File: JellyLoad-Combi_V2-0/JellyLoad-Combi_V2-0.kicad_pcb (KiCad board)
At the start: 2 copper layers, 26 x 35 mm, 26 parts, among them J1 Conn_02x07_Odd_Even, Q1 SFH3710, Q2 SFH3710, Q3 SFH3710, Q4 SFH3710, Q5 SFH3710, Q6 SFH3710, Q7 SFH3710, Q8 SFH3710, Q9 SFH3710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

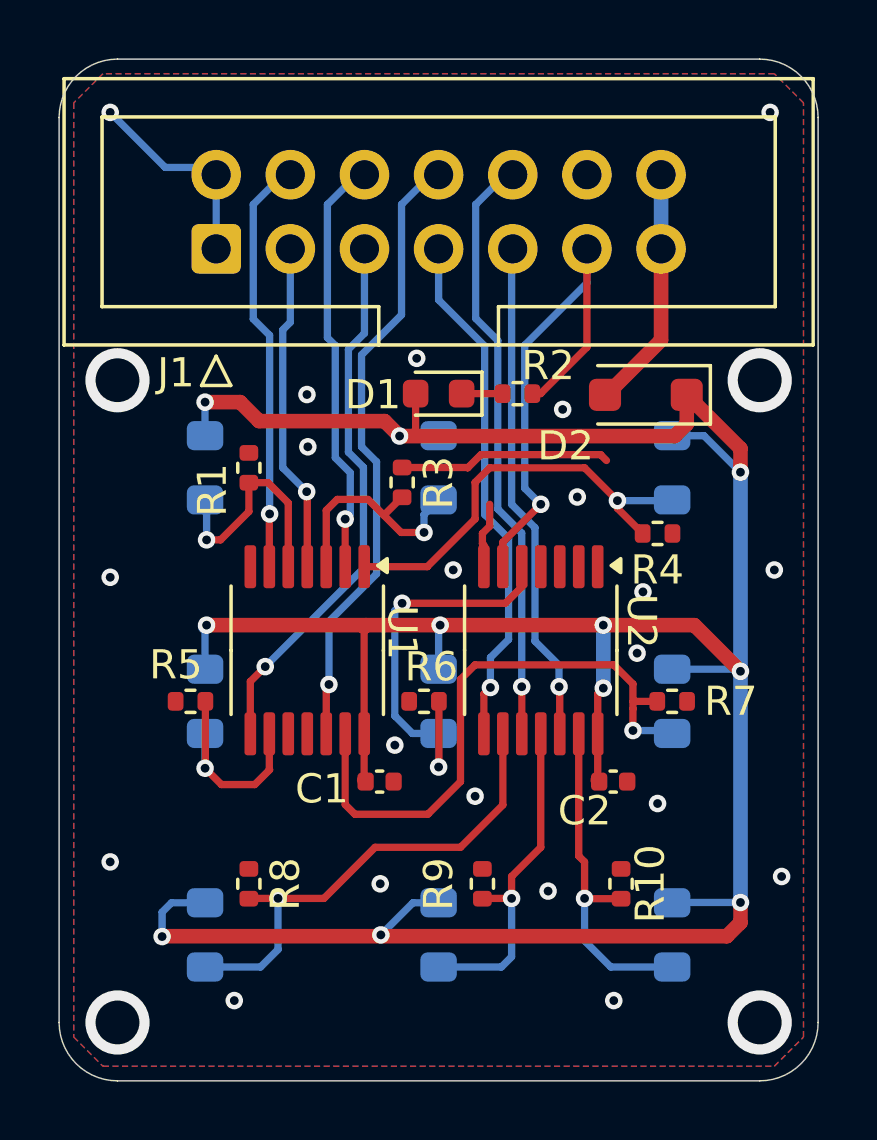
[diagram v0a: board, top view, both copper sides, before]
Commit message: Layout updates for manufacture process
Corner mounting holes widened to 2.0mm for more robust mechanics. Added 2x tooling holes (1.152mm) for assembly process.
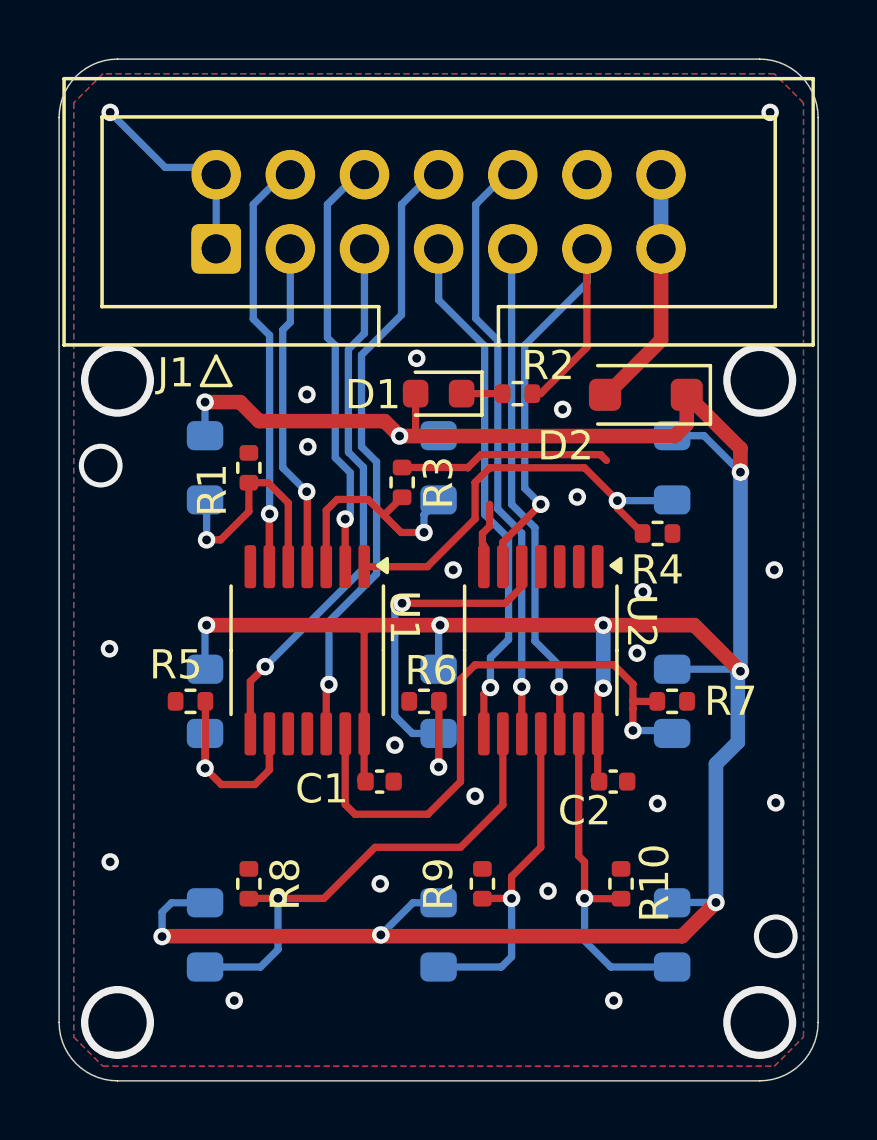
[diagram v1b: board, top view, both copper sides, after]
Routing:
- net VCC: track 106.7 -> 105.0 mm
- net GND: vias 25 -> 27
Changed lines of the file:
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@@
 		(grid_origin 170 107)
 		(pcbplotparams
-			(layerselection 0x00014dc_ffffffff)
-			(plot_on_all_layers_selection 0x0000000_00000000)
+			(layerselection 0x00010dc_ffffffff)
+			(plot_on_all_layers_selection 0x0001000_00000000)
 			(disableapertmacros no)
 			(usegerberextensions no)
@@
 		(tags "resistor")
 		(property "Reference" "R10"
-			(at 0 1 90)
+			(at 0.025 1.15 90)
 			(layer "F.SilkS")
 			(effects
@@
 		(tags "TSSOP SO")
 		(property "Reference" "U1"
-			(at -0.606 -3.25 -90)
+			(at -1.125 -3.325 -90)
 			(unlocked yes)
 			(layer "F.SilkS")
@@
 		(tags "resistor")
 		(property "Reference" "R6"
-			(at -0.25 1.182 0)
+			(at -0.25 1.05 0)
 			(layer "F.SilkS")
 			(effects
@@
 	)
 	(via
-		(at 158.75 102.75)
+		(at 181.55 110.475)
 		(size 0.6)
 		(drill 0.3)
@@
 	)
 	(via
+		(at 158.425 98.925)
+		(size 1.5)
+		(drill 1.152)
+		(layers "F.Cu" "B.Cu")
+		(net 1)
+	)
+	(via
 		(at 181.356 86.8255)
 		(size 0.6)
@@
 	(via
 		(at 159 96)
-		(size 2.2)
-		(drill 1.5)
+		(size 2.5)
+		(drill 2)
 		(layers "F.Cu" "B.Cu")
 		(net 1)
@@
 	(via
 		(at 181 96)
-		(size 2.2)
-		(drill 1.5)
+		(size 2.5)
+		(drill 2)
 		(layers "F.Cu" "B.Cu")
 		(net 1)
@@
 	(via
 		(at 181 118)
-		(size 2.2)
-		(drill 1.5)
+		(size 2.5)
+		(drill 2)
 		(layers "F.Cu" "B.Cu")
 		(net 1)
@@
 	)
 	(via
-		(at 181.75 113)
-		(size 0.6)
-		(drill 0.3)
+		(at 181.55 115.05)
+		(size 1.5)
+		(drill 1.152)
 		(layers "F.Cu" "B.Cu")
 		(net 1)
@@
 	)
 	(via
+		(at 158.725 105.2)
+		(size 0.6)
+		(drill 0.3)
+		(layers "F.Cu" "B.Cu")
+		(net 1)
+	)
+	(via
 		(at 158.75 86.8255)
 		(size 0.6)
@@
 	(via
 		(at 159 118)
-		(size 2.2)
-		(drill 1.5)
+		(size 2.5)
+		(drill 2)
 		(layers "F.Cu" "B.Cu")
 		(net 1)
@@
 	)
 	(segment
-		(start 168.663 97.913)
-		(end 178.087 97.913)
+		(start 179.5 113.89)
+		(end 178.344 115.046)
 		(width 0.5)
 		(layer "F.Cu")
@@
 	)
 	(segment
-		(start 179.874 115.046)
-		(end 160.54 115.046)
+		(start 168.663 97.913)
+		(end 178.087 97.913)
 		(width 0.5)
 		(layer "F.Cu")
@@
 	)
 	(segment
-		(start 180.34 114.58)
-		(end 179.874 115.046)
-		(width 0.5)
-		(layer "F.Cu")
-		(net 2)
-	)
-	(segment
 		(start 167.45 108.1125)
 		(end 167.45 104.453)
@@
 	)
 	(segment
-		(start 160.54 115.046)
-		(end 160.528 115.058)
-		(width 0.5)
-		(layer "F.Cu")
-		(net 2)
-	)
-	(segment
 		(start 168.663 97.913)
 		(end 168.15 97.4)
@@
 	)
 	(segment
-		(start 180.34 113.89)
-		(end 180.34 114.58)
+		(start 178.5 97.5)
+		(end 178.5 96.5)
 		(width 0.5)
 		(layer "F.Cu")
@@
 	)
 	(segment
-		(start 178.5 97.5)
-		(end 178.5 96.5)
+		(start 178.344 115.046)
+		(end 160.54 115.046)
 		(width 0.5)
 		(layer "F.Cu")
@@
 	)
 	(segment
+		(start 160.54 115.046)
+		(end 160.528 115.058)
+		(width 0.5)
+		(layer "F.Cu")
+		(net 2)
+	)
+	(segment
 		(start 167.513 104.39)
 		(end 162.052 104.39)
@@
 	)
 	(via
-		(at 180.34 113.89)
+		(at 179.5 113.89)
 		(size 0.6)
 		(drill 0.3)
@@
 	)
 	(segment
+		(start 178.01 113.89)
+		(end 178 113.9)
+		(width 0.25)
+		(layer "B.Cu")
+		(net 2)
+	)
+	(segment
 		(start 168.676 97.9)
 		(end 170 97.9)
@@
 	)
 	(segment
-		(start 180.34 105.97)
-		(end 180.34 113.89)
-		(width 0.5)
+		(start 168.021 115)
+		(end 169.121 113.9)
+		(width 0.25)
 		(layer "B.Cu")
 		(net 2)
 	)
 	(segment
-		(start 168.021 115)
-		(end 169.121 113.9)
-		(width 0.25)
+		(start 179.5 113.89)
+		(end 179.5 109.15)
+		(width 0.5)
 		(layer "B.Cu")
 		(net 2)
@@
 	)
 	(segment
-		(start 178.01 113.89)
-		(end 178 113.9)
-		(width 0.25)
-		(layer "B.Cu")
-		(net 2)
-	)
-	(segment
 		(start 160.85 113.9)
 		(end 160.528 114.222)
@@
 	)
 	(segment
+		(start 180.25 108.4)
+		(end 180.25 106.06)
+		(width 0.5)
+		(layer "B.Cu")
+		(net 2)
+	)
+	(segment
 		(start 180.34 105.97)
 		(end 180.34 99.15)
@@
 	)
 	(segment
+		(start 179.5 109.15)
+		(end 180.25 108.4)
+		(width 0.5)
+		(layer "B.Cu")
+		(net 2)
+	)
+	(segment
 		(start 169.121 113.9)
 		(end 170 113.9)
@@
 	)
 	(segment
-		(start 180.34 113.89)
-		(end 178.01 113.89)
+		(start 180.27 105.9)
+		(end 178 105.9)
 		(width 0.25)
 		(layer "B.Cu")
@@
 	)
 	(segment
-		(start 180.27 105.9)
-		(end 178 105.9)
+		(start 179.5 113.89)
+		(end 178.01 113.89)
 		(width 0.25)
 		(layer "B.Cu")
@@
 		(layer "B.Cu")
 		(net 2)
+	)
+	(segment
+		(start 180.25 106.06)
+		(end 180.34 105.97)
+		(width 0.5)
+		(layer "B.Cu")
+		(net 2)

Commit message: Admin updates to schematic and layout
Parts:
- Q1, Q2, Q3, Q4, Q5, Q6, Q7, Q8, Q9: value SFH3710 -> SFH3710-4
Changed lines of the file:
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@@
 		(grid_origin 170 107)
 		(pcbplotparams
-			(layerselection 0x00010dc_ffffffff)
+			(layerselection 0x0001000_7fffffff)
 			(plot_on_all_layers_selection 0x0001000_00000000)
 			(disableapertmacros no)
@@
 			(psnegative no)
 			(psa4output no)
-			(plotreference yes)
-			(plotvalue yes)
-			(plotfptext yes)
+			(plotreference no)
+			(plotvalue no)
+			(plotfptext no)
 			(plotinvisibletext no)
 			(sketchpadsonfab no)
 			(subtractmaskfromsilk no)
-			(outputformat 1)
+			(outputformat 5)
 			(mirror no)
 			(drillshape 0)
@@
 			)
 		)
+		(property "DK-PN" "1727-3880-1-ND"
+			(at 0 0 180)
+			(unlocked yes)
+			(layer "F.Fab")
+			(hide yes)
+			(effects
+				(font
+					(size 1 1)
+					(thickness 0.15)
+				)
+			)
+		)
 		(property ki_fp_filters "D*SOD?123F*")
 		(sheetname "Root")
@@
 			)
 		)
+		(property "DK-PN" "490-6328-1-ND"
+			(at 0 0 0)
+			(unlocked yes)
+			(layer "F.Fab")
+			(hide yes)
+			(effects
+				(font
+					(size 1 1)
+					(thickness 0.15)
+				)
+			)
+		)
 		(property ki_fp_filters "C_*")
 		(sheetname "Root")
@@
 			)
 		)
+		(property "DK-PN" "296-8234-1-ND"
+			(at 0 0 -90)
+			(unlocked yes)
+			(layer "F.Fab")
+			(hide yes)
+			(effects
+				(font
+					(size 1 1)
+					(thickness 0.15)
+				)
+			)
+		)
 		(property ki_fp_filters "DIP*W7.62mm*")
 		(sheetname "Root")
@@
 			)
 		)
+		(property "DK-PN" "490-6328-1-ND"
+			(at 0 0 0)
+			(unlocked yes)
+			(layer "F.Fab")
+			(hide yes)
+			(effects
+				(font
+					(size 1 1)
+					(thickness 0.15)
+				)
+			)
+		)
 		(property ki_fp_filters "C_*")
 		(sheetname "Root")
@@
 			)
 		)
+		(property "DK-PN" "2987-CH87142V201-ND"
+			(at 0 0 90)
+			(unlocked yes)
+			(layer "F.Fab")
+			(hide yes)
+			(effects
+				(font
+					(size 1 1)
+					(thickness 0.15)
+				)
+			)
+		)
 		(property ki_fp_filters "Connector*:*_2x??_*")
 		(sheetname "Root")
@@
 			)
 		)
+		(property "DK-PN" "296-8234-1-ND"
+			(at 0 0 -90)
+			(unlocked yes)
+			(layer "F.Fab")
+			(hide yes)
+			(effects
+				(font
+					(size 1 1)
+					(thickness 0.15)
+				)
+			)
+		)
 		(property ki_fp_filters "DIP*W7.62mm*")
 		(sheetname "Root")
@@
 			)
 		)
+		(property "DK-PN" "732-4978-1-ND"
+			(at 0 0 180)
+			(unlocked yes)
+			(layer "F.Fab")
+			(hide yes)
+			(effects
+				(font
+					(size 1 1)
+					(thickness 0.15)
+				)
+			)
+		)
 		(property ki_fp_filters "LED* LED_SMD:* LED_THT:*")
 		(sheetname "Root")
@@
 			)
 		)
-		(property "Value" "SFH3710"
+		(property "Value" "SFH3710-4"
 			(at 0 -1.8 90)
 			(unlocked yes)
@@
 			)
 		)
+		(property "DK-PN" "475-SFH3710-3/4-ZCT-ND"
+			(at 0 0 -90)
+			(unlocked yes)
+			(layer "B.Fab")
+			(hide yes)
+			(effects
+				(font
+					(size 1 1)
+					(thickness 0.15)
+				)
+				(justify mirror)
+			)
+		)
 		(property ki_fp_filters "LED?SMD:LED?PLCC?2?3.4x3.0mm?KA*")
 		(sheetname "Root")
@@
 			)
 		)
-		(property "Value" "SFH3710"
+		(property "Value" "SFH3710-4"
 			(at 0 -1.8 90)
 			(unlocked yes)
@@
 			)
 		)
+		(property "DK-PN" "475-SFH3710-3/4-ZCT-ND"
+			(at 0 0 -90)
+			(unlocked yes)
+			(layer "B.Fab")
+			(hide yes)
+			(effects
+				(font
+					(size 1 1)
+					(thickness 0.15)
+				)
+				(justify mirror)
+			)
+		)
 		(property ki_fp_filters "LED?SMD:LED?PLCC?2?3.4x3.0mm?KA*")
 		(sheetname "Root")
@@
 			)
 		)
-		(property "Value" "SFH3710"
+		(property "Value" "SFH3710-4"
 			(at 0 -1.8 90)
 			(unlocked yes)
@@
 			)
 		)
+		(property "DK-PN" "475-SFH3710-3/4-ZCT-ND"
+			(at 0 0 -90)
+			(unlocked yes)
+			(layer "B.Fab")
+			(hide yes)
+			(effects
+				(font
+					(size 1 1)
+					(thickness 0.15)
+				)
+				(justify mirror)
+			)
+		)
 		(property ki_fp_filters "LED?SMD:LED?PLCC?2?3.4x3.0mm?KA*")
 		(sheetname "Root")
@@
 			)
 		)
-		(property "Value" "SFH3710"
+		(property "Value" "SFH3710-4"
 			(at 0 -1.8 90)
 			(unlocked yes)
@@
 			)
 		)
+		(property "DK-PN" "475-SFH3710-3/4-ZCT-ND"
+			(at 0 0 -90)
+			(unlocked yes)
+			(layer "B.Fab")
+			(hide yes)
+			(effects
+				(font
+					(size 1 1)
+					(thickness 0.15)
+				)
+				(justify mirror)
+			)
+		)
 		(property ki_fp_filters "LED?SMD:LED?PLCC?2?3.4x3.0mm?KA*")
 		(sheetname "Root")
@@
 			)
 		)
-		(property "Value" "SFH3710"
+		(property "Value" "SFH3710-4"
 			(at 0 -1.8 90)
 			(unlocked yes)
@@
 			)
 		)
+		(property "DK-PN" "475-SFH3710-3/4-ZCT-ND"
+			(at 0 0 -90)
+			(unlocked yes)
+			(layer "B.Fab")
+			(hide yes)
+			(effects
+				(font
+					(size 1 1)
+					(thickness 0.15)
+				)
+				(justify mirror)
+			)
+		)
 		(property ki_fp_filters "LED?SMD:LED?PLCC?2?3.4x3.0mm?KA*")
 		(sheetname "Root")
@@
 			)
 		)
-		(property "Value" "SFH3710"
+		(property "Value" "SFH3710-4"
 			(at 0 -1.8 90)
 			(unlocked yes)
@@
 			)
 		)
+		(property "DK-PN" "475-SFH3710-3/4-ZCT-ND"
+			(at 0 0 -90)
+			(unlocked yes)
+			(layer "B.Fab")
+			(hide yes)
+			(effects
+				(font
+					(size 1 1)
+					(thickness 0.15)
+				)
+				(justify mirror)
+			)
+		)
 		(property ki_fp_filters "LED?SMD:LED?PLCC?2?3.4x3.0mm?KA*")
 		(sheetname "Root")
@@
 			)
 		)
-		(property "Value" "SFH3710"
+		(property "Value" "SFH3710-4"
 			(at 0 -1.8 90)
 			(unlocked yes)
@@
 			)
 		)
+		(property "DK-PN" "475-SFH3710-3/4-ZCT-ND"
+			(at 0 0 -90)
+			(unlocked yes)
+			(layer "B.Fab")
+			(hide yes)
+			(effects
+				(font
+					(size 1 1)
+					(thickness 0.15)
+				)
+				(justify mirror)
+			)
+		)
 		(property ki_fp_filters "LED?SMD:LED?PLCC?2?3.4x3.0mm?KA*")
 		(sheetname "Root")
@@
 			)
 		)
-		(property "Value" "SFH3710"
+		(property "Value" "SFH3710-4"
 			(at 0 -1.8 90)
 			(unlocked yes)
@@
 			)
 		)
+		(property "DK-PN" "475-SFH3710-3/4-ZCT-ND"
+			(at 0 0 -90)
+			(unlocked yes)
+			(layer "B.Fab")
+			(hide yes)
+			(effects
+				(font
+					(size 1 1)
+					(thickness 0.15)
+				)
+				(justify mirror)
+			)
+		)
 		(property ki_fp_filters "LED?SMD:LED?PLCC?2?3.4x3.0mm?KA*")
 		(sheetname "Root")
@@
 			)
 		)
-		(property "Value" "SFH3710"
+		(property "Value" "SFH3710-4"
 			(at 0 -1.8 90)
 			(unlocked yes)
@@
 					(thickness 0.15)
 				)
+				(justify mirror)
+			)
+		)
+		(property "DK-PN" "475-SFH3710-3/4-ZCT-ND"
+			(at 0 0 -90)
+			(unlocked yes)
+			(layer "B.Fab")
+			(hide yes)
+			(effects
+				(font
+					(size 1 1)
+					(thickness 0.15)
+				)
